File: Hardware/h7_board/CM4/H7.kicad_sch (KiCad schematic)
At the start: 34 parts, among them J3 SWDIO, J4 Micro_SD_Card, J7 USART, U2 STM32H743VITx, Y1 16MHz

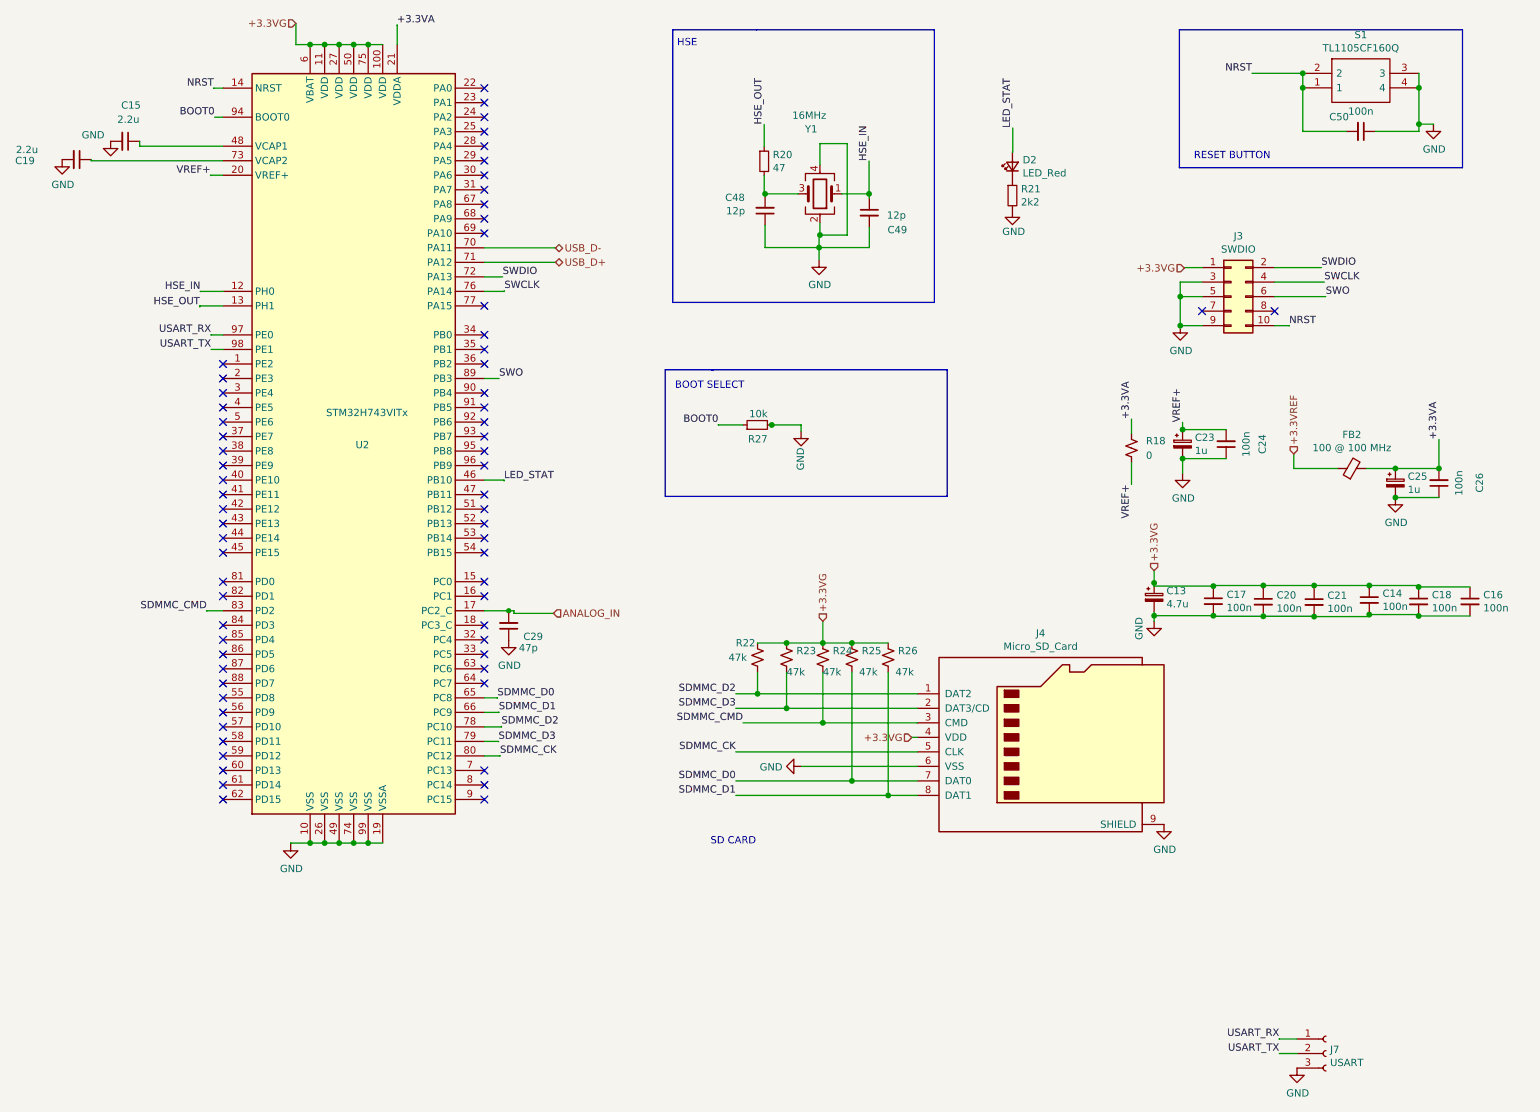
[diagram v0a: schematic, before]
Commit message: Edited Design to modify to LDO regulator and improve board layout
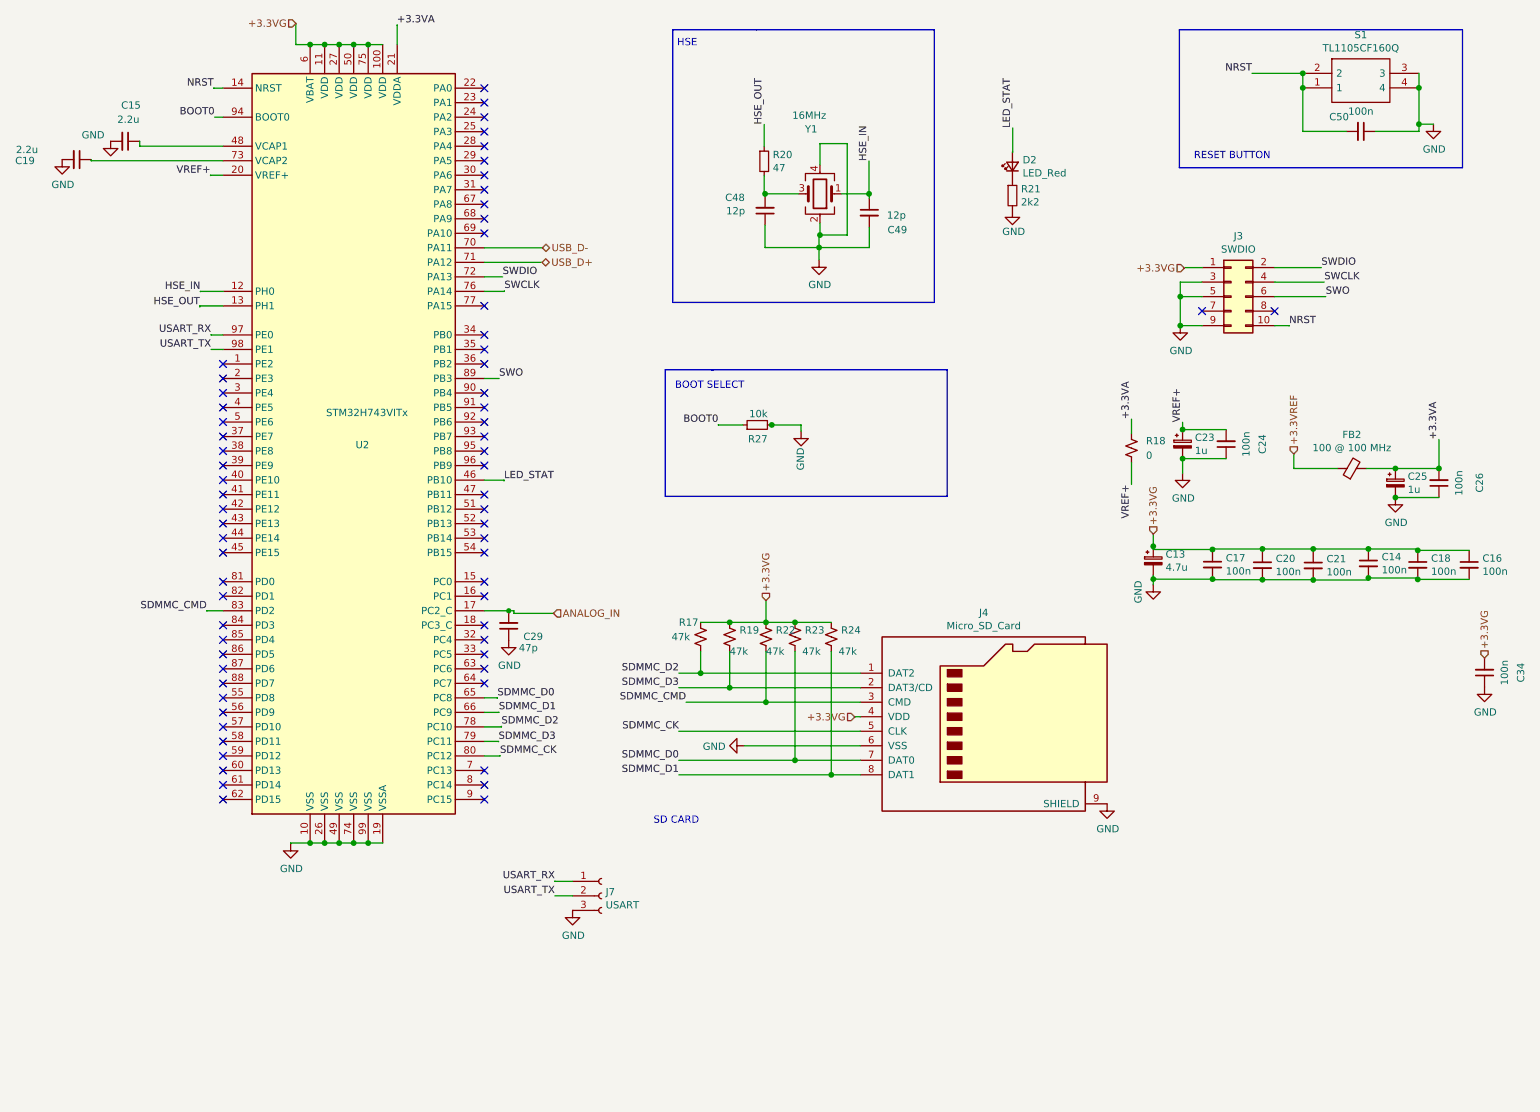
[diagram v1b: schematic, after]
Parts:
- removed R25, R26: 47k, Resistor_SMD:R_0402_1005Metric, symbol Device:R_Small_US
- added C34: 100n, Capacitor_SMD:C_0402_1005Metric, symbol Device:C_Small
- added R17, R19: 47k, Resistor_SMD:R_0402_1005Metric, symbol Device:R_Small_US
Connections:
- net +3.3VG: now also C34.2, R17.2, R19.2
- net GND: now also C34.1
- net SDMMC_CMD: now also R22.1; no longer R24.1
- net SDMMC_D0: now also R23.1
- net SDMMC_D1: now also R24.1
- net SDMMC_D2: now also R17.1; no longer R22.1
- net SDMMC_D3: now also R19.1; no longer R23.1
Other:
- moved on the sheet: C13, C14, C16, C17, C18, C20, C21, J7
